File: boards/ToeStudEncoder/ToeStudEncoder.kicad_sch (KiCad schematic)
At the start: 19 parts, among them J1 Swell, J2 ISP, J3 ToeLeft, J4 ToeRight, J5 MIDI Out, J6 Controller, J7 Pedal, J8 MIDI In, U1 ATmega48-20P, U2 6N138

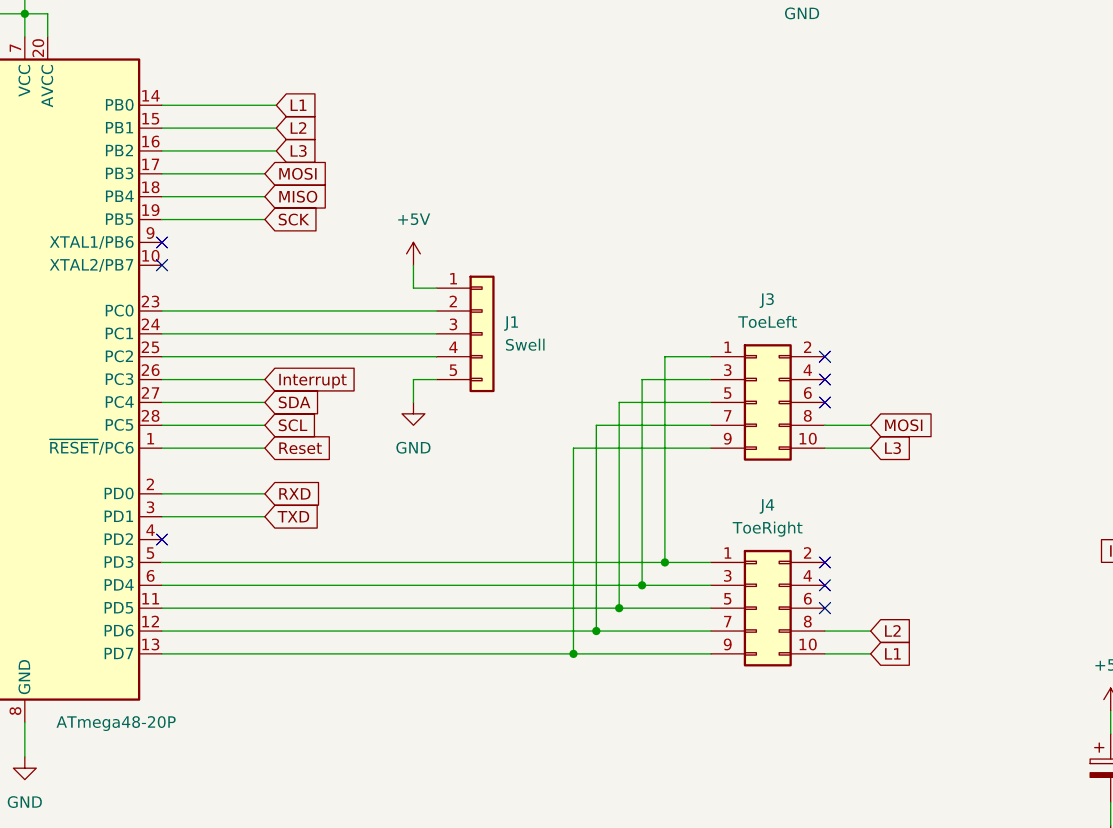
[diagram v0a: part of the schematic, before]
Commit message: Renamed toestud encoder schematics
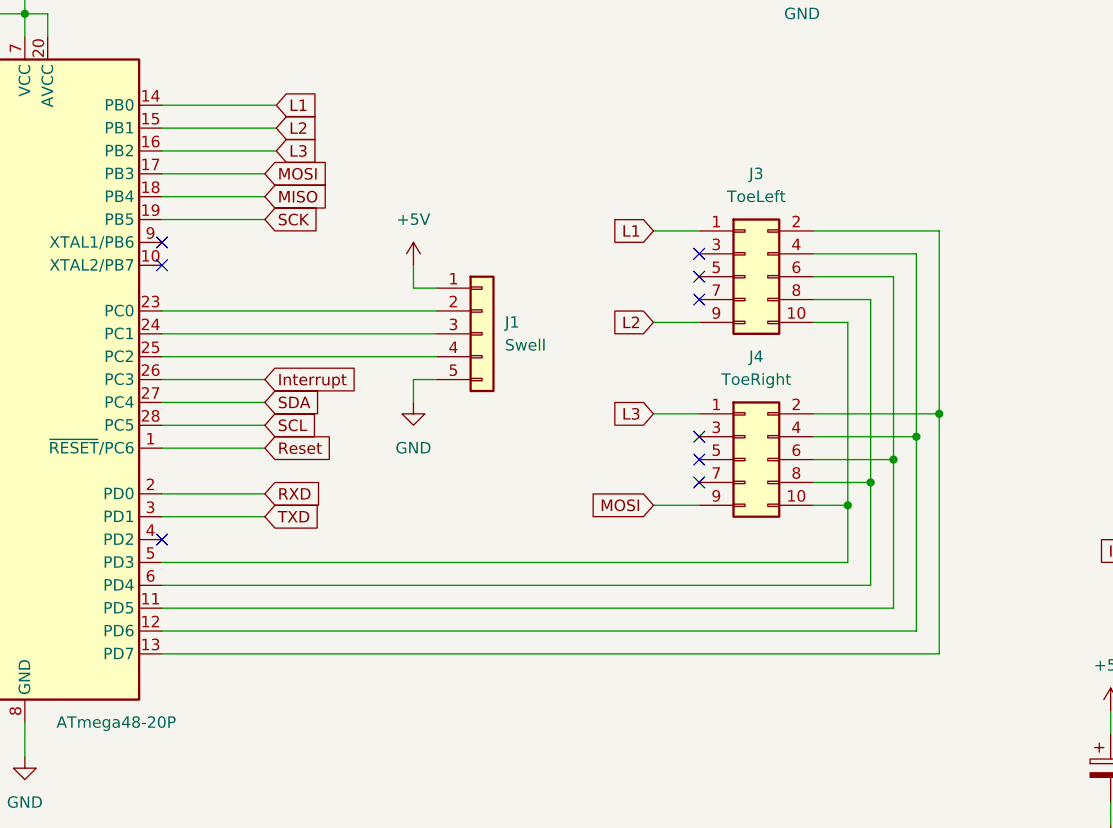
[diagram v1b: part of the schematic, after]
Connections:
- net L1: now also J3.1 (Pin_1); no longer J4.10 (Pin_10)
- net L2: now also J3.9 (Pin_9); no longer J4.8 (Pin_8)
- net L3: now also J4.1 (Pin_1); no longer J3.10 (Pin_10)
- net MOSI: now also J4.9 (Pin_9); no longer J3.8 (Pin_8)
- net at J4.2 (Pin_2): now also J3.2 (Pin_2), U1.13 (PD7)
- net at J4.4 (Pin_4): now also J3.4 (Pin_4), U1.12 (PD6)
- net at J4.6 (Pin_6): now also J3.6 (Pin_6), U1.11 (PD5)
- new net: J3.10 (Pin_10), J4.10 (Pin_10), U1.5 (PD3)
- new net: J3.8 (Pin_8), J4.8 (Pin_8), U1.6 (PD4)
- now unconnected: J3.3 (Pin_3), J3.5 (Pin_5), J3.7 (Pin_7), J4.3 (Pin_3), J4.5 (Pin_5), J4.7 (Pin_7)
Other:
- moved on the sheet: J3, J4

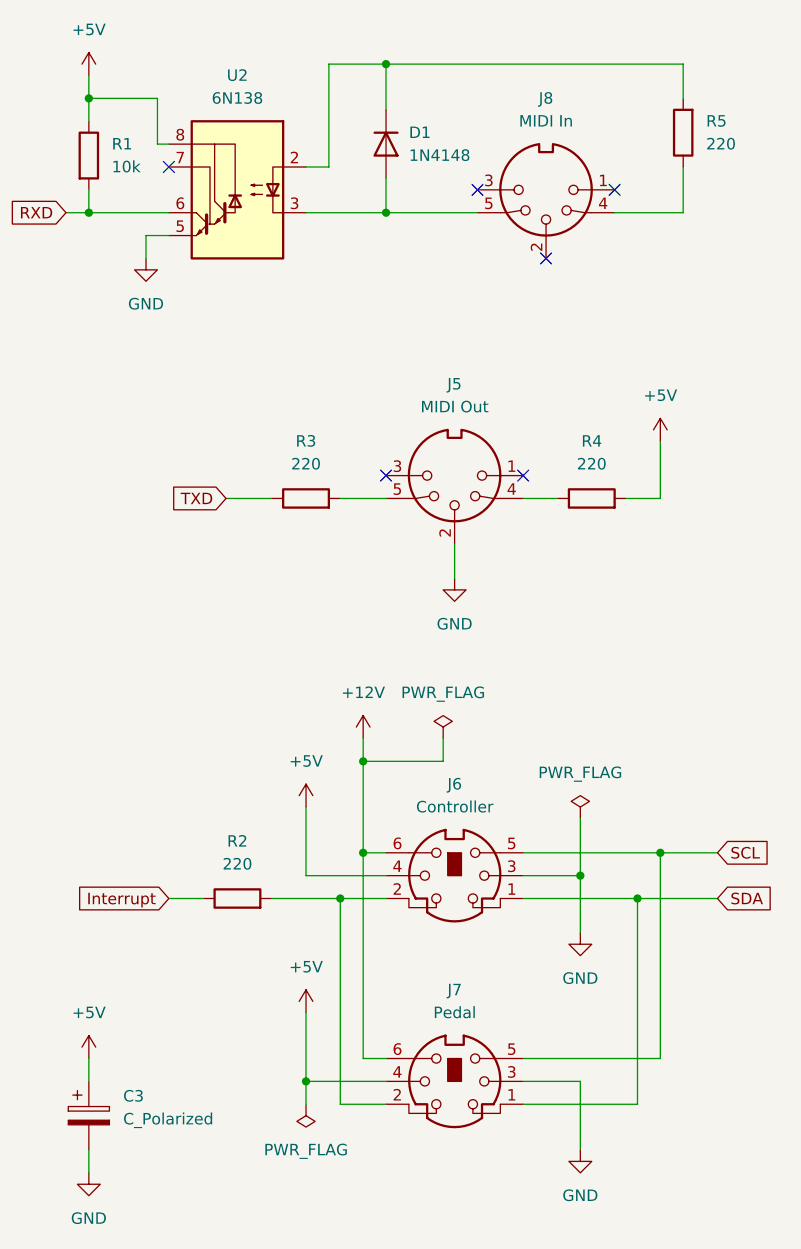
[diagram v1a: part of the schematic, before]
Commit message: Updated Pedal Encoder to use UART from ToeStudEncoder
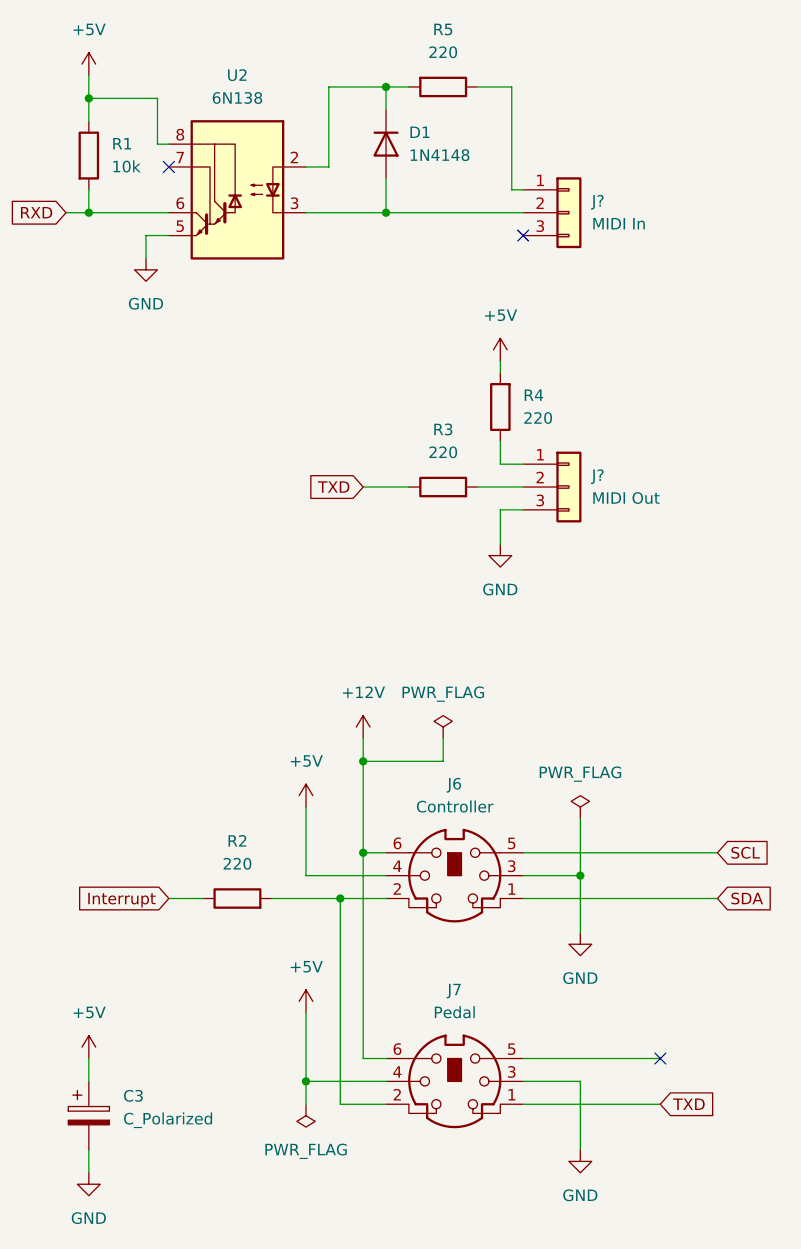
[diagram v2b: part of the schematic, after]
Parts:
- removed J5: MIDI Out, symbol Connector:DIN-5_180degree
- removed J8: MIDI In, symbol Connector:DIN-5_180degree
- added J?: MIDI In, symbol Connector_Generic:Conn_01x03
- added J?: MIDI Out, symbol Connector_Generic:Conn_01x03
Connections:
- net GND: now also J?.3 (Pin_3)
- net SCL: no longer J7.5
- net SDA: no longer J7.1
- net TXD: now also J7.1
- net at R4.1: now also J?.1 (Pin_1)
- net at R3.2: now also J?.2 (Pin_2)
- net at R5.1: now also J?.1 (Pin_1)
- net at D1.2 (A), U2.3 (C2): now also J?.2 (Pin_2)
- no-connect marks 16 -> 13
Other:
- moved on the sheet: R3, R4, R5

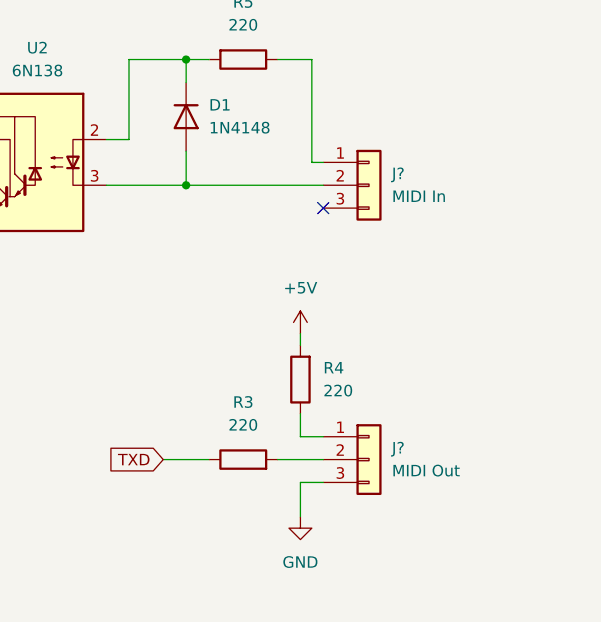
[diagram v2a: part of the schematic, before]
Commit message: Renamed PCBs and updated to KiCAD 7.0
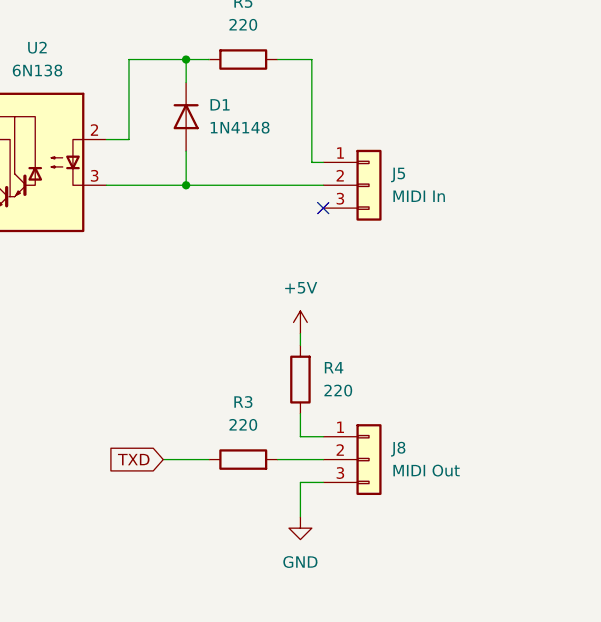
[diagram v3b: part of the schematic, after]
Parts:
- C1, C2: footprint (none) -> Capacitor_THT:C_Disc_D7.5mm_W2.5mm_P5.00mm
- C3: footprint (none) -> Capacitor_THT:CP_Radial_D10.0mm_P5.00mm
- J1: footprint (none) -> Connector_JST:JST_XH_B5B-XH-A_1x05_P2.50mm_Vertical
- J5, J8: renamed from J?; footprint (none) -> Connector_PinHeader_2.54mm:PinHeader_1x03_P2.54mm_Vertical

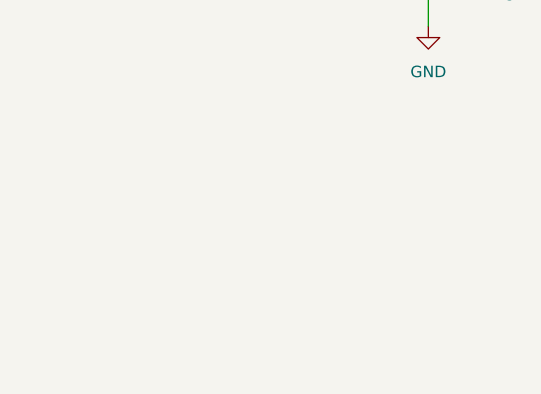
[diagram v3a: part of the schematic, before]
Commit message: Added output buffer to MIDI outputs
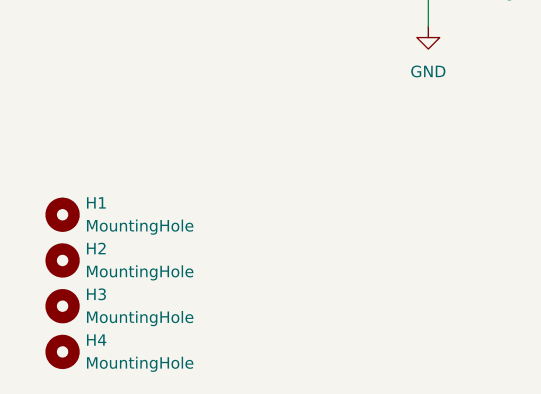
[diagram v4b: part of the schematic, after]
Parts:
- added H1, H2, H3, H4: MountingHole, MountingHole:MountingHole_3mm, symbol Mechanical:MountingHole
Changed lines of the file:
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@@
+    )
+  )
+  (symbol (lib_id "Mechanical:MountingHole") (at 30.48 170.815 0) (unit 1)
+    (in_bom yes) (on_board yes) (dnp no) (fields_autoplaced)
+    (property "Reference" "H3" (at 33.02 169.545 0)
+      (effects (font (size 1.27 1.27)) (justify left))
+    )
+    (property "Value" "MountingHole" (at 33.02 172.085 0)
+      (effects (font (size 1.27 1.27)) (justify left))
+    )
+    (property "Footprint" "MountingHole:MountingHole_3mm" (at 30.48 170.815 0)
+      (effects (font (size 1.27 1.27)) hide)
+    )
+    (property "Datasheet" "~" (at 30.48 170.815 0)
+      (effects (font (size 1.27 1.27)) hide)
+    )
+    (instances
+      (project "ToeStudEncoder"
+        (path "/a0f642fd-a17d-4032-8879-54d542360da8"
+          (reference "H3") (unit 1)
+        )
+      )
     )
   )
@@
     )
   )
+  (symbol (lib_id "Mechanical:MountingHole") (at 30.48 160.655 0) (unit 1)
+    (in_bom yes) (on_board yes) (dnp no) (fields_autoplaced)
+    (property "Reference" "H1" (at 33.02 159.385 0)
+      (effects (font (size 1.27 1.27)) (justify left))
+    )
+    (property "Value" "MountingHole" (at 33.02 161.925 0)
+      (effects (font (size 1.27 1.27)) (justify left))
+    )
+    (property "Footprint" "MountingHole:MountingHole_3mm" (at 30.48 160.655 0)
+      (effects (font (size 1.27 1.27)) hide)
+    )
+    (property "Datasheet" "~" (at 30.48 160.655 0)
+      (effects (font (size 1.27 1.27)) hide)
+    )
+    (instances
+      (project "ToeStudEncoder"
+        (path "/a0f642fd-a17d-4032-8879-54d542360da8"
+          (reference "H1") (unit 1)
+        )
+      )
+    )
+  )
   (symbol (lib_id "power:GND") (at 198.12 45.72 0) (unit 1)
     (in_bom yes) (on_board yes) (dnp no) (fields_autoplaced)
@@
         (path "/a0f642fd-a17d-4032-8879-54d542360da8"
           (reference "#FLG0103") (unit 1)
+        )
+      )
+    )
+  )
+  (symbol (lib_id "Mechanical:MountingHole") (at 30.48 165.735 0) (unit 1)
+    (in_bom yes) (on_board yes) (dnp no) (fields_autoplaced)
+    (property "Reference" "H2" (at 33.02 164.465 0)
+      (effects (font (size 1.27 1.27)) (justify left))
+    )
+    (property "Value" "MountingHole" (at 33.02 167.005 0)
+      (effects (font (size 1.27 1.27)) (justify left))
+    )
+    (property "Footprint" "MountingHole:MountingHole_3mm" (at 30.48 165.735 0)
+      (effects (font (size 1.27 1.27)) hide)
+    )
+    (property "Datasheet" "~" (at 30.48 165.735 0)
+      (effects (font (size 1.27 1.27)) hide)
+    )
+    (instances
+      (project "ToeStudEncoder"
+        (path "/a0f642fd-a17d-4032-8879-54d542360da8"
+          (reference "H2") (unit 1)
         )
       )
@@
         )
       )
+    )
+  )
+  (symbol (lib_id "Mechanical:MountingHole") (at 30.48 175.895 0) (unit 1)
+    (in_bom yes) (on_board yes) (dnp no) (fields_autoplaced)
+    (property "Reference" "H4" (at 33.02 174.625 0)
+      (effects (font (size 1.27 1.27)) (justify left))
+    )
+    (property "Value" "MountingHole" (at 33.02 177.165 0)
+      (effects (font (size 1.27 1.27)) (justify left))
+    )
+    (property "Footprint" "MountingHole:MountingHole_3mm" (at 30.48 175.895 0)
+      (effects (font (size 1.27 1.27)) hide)
+    )
+    (property "Datasheet" "~" (at 30.48 175.895 0)
+      (effects (font (size 1.27 1.27)) hide)
+    )
+    (instances
+      (project "ToeStudEncoder"
+        (path "/a0f642fd-a17d-4032-8879-54d542360da8"
+          (reference "H4") (unit 1)
+        )
+      )
